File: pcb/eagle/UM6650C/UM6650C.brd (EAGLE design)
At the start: 20.9 x 28.2 mm, 11 parts, among them U1 74HC139, U2 74HC00, U3 74HC373, U4 28C64AVS

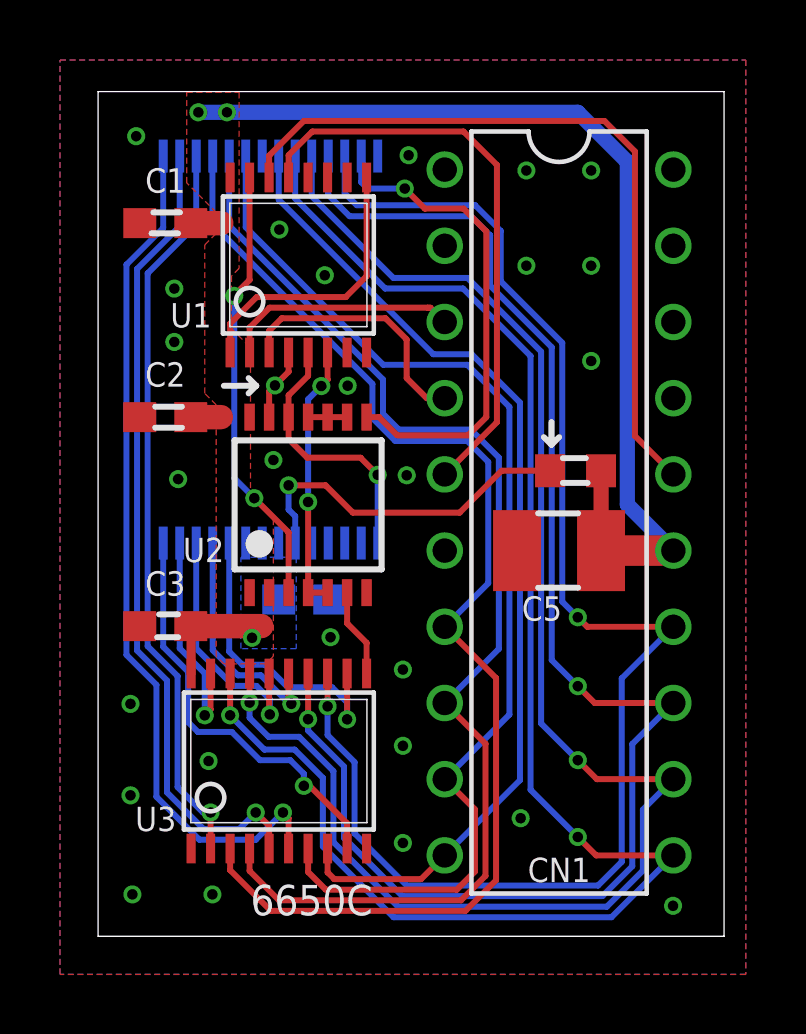
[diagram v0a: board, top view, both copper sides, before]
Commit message: Add Multitap schematic and board file
Update UM6650C board file
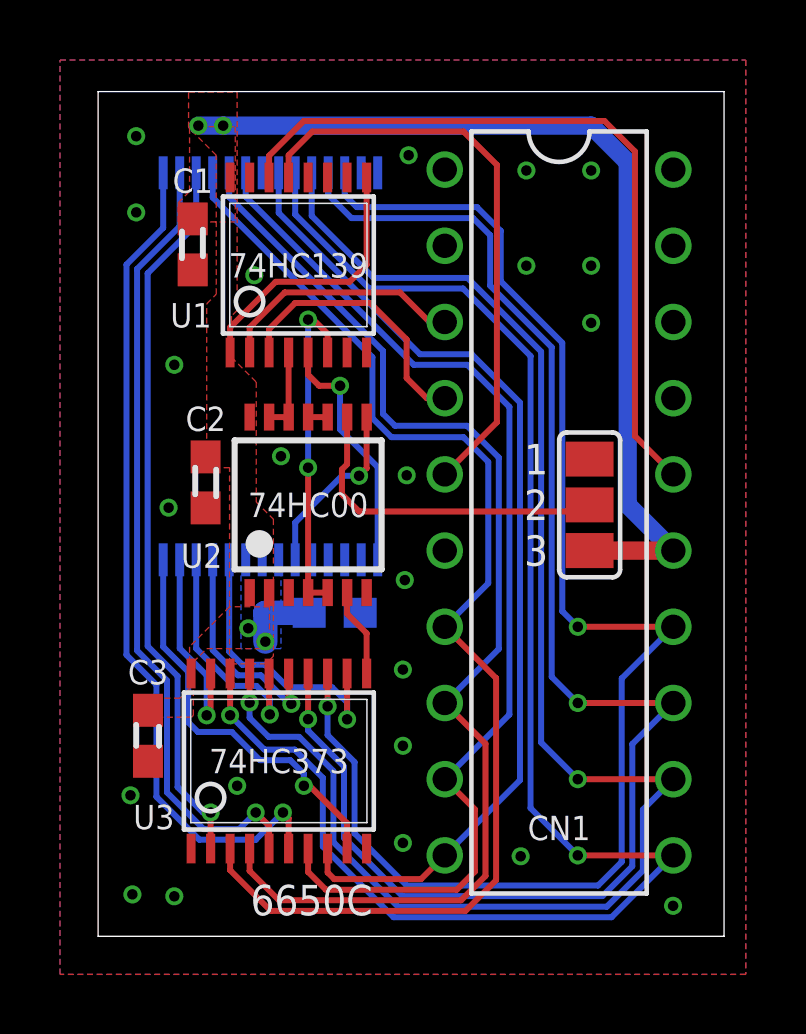
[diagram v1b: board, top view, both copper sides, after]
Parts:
- removed C5: (no value), rcl:C1210
- removed R1: 10K, rcl:R0603
- added SJ1: (no value), jumper:SJ_2
- moved C3 3.70 mm to (1.66, 6.68), turned to 270 degrees
- moved C2 2.56 mm to (3.59, 15.1), turned to 270 degrees
- moved C1 1.16 mm to (3.15, 23.1), turned to 270 degrees
- moved C4 1.11 mm to (7.89, 10.8)
- moved U4 0.56 mm to (5.75, 19.0)
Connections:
- removed net !CE: U2.8, U4.20
- removed net N$4: U1.15, U2.3
- new net EN: SJ1.2, U2.9
- net !OE: no longer U2.12
- net !WE: now also U2.12
- net !WE': now also U2.8; no longer R1.1
- net GND: now also SJ1.1, U1.15, U4.20; no longer C5.2
- net N$1: no longer U2.9
- net VCC: now also SJ1.3; no longer C5.1, R1.2
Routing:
- net !CE: track 16.4 -> 0.00 mm, vias 1 -> 0
- net N$4: track 14.8 -> 0.00 mm, vias 2 -> 0
- net EN: track 0.00 -> 11.2 mm
- net VCC: track 39.6 -> 33.6 mm, vias 3 -> 4
- net !WE': track 11.7 -> 6.08 mm
- net N$3: track 8.92 -> 11.2 mm
- net D2: track 37.3 -> 36.1 mm
- net D0: track 41.5 -> 40.7 mm
- net N$1: track 1.30 -> 0.65 mm
- net !OE: track 8.89 -> 8.28 mm
- net D1: track 39.8 -> 39.2 mm
- net CA2: track 28.7 -> 28.2 mm
- net CA1: track 27.3 -> 26.7 mm
- net CA0: track 24.8 -> 24.2 mm
- net CA7: track 10.3 -> 9.79 mm
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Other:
- board text added: "1 2 3"
- board text added: "1-2 WRITE DISABLE 2-3 WRITE ENABLE"
- board text added: "28C64B"
